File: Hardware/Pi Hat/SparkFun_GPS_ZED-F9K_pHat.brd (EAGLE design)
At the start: 65 x 56.5 mm, 70 parts, among them J1 QWIIC_RIGHT_ANGLE, J2 RASPBERRYPI-40-PIN-GPIO_PTH_N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, J4 U.FL, U1 UBLOX_ZED_F9K, U3 TRIPLE_BUFFER_74LVC3G07

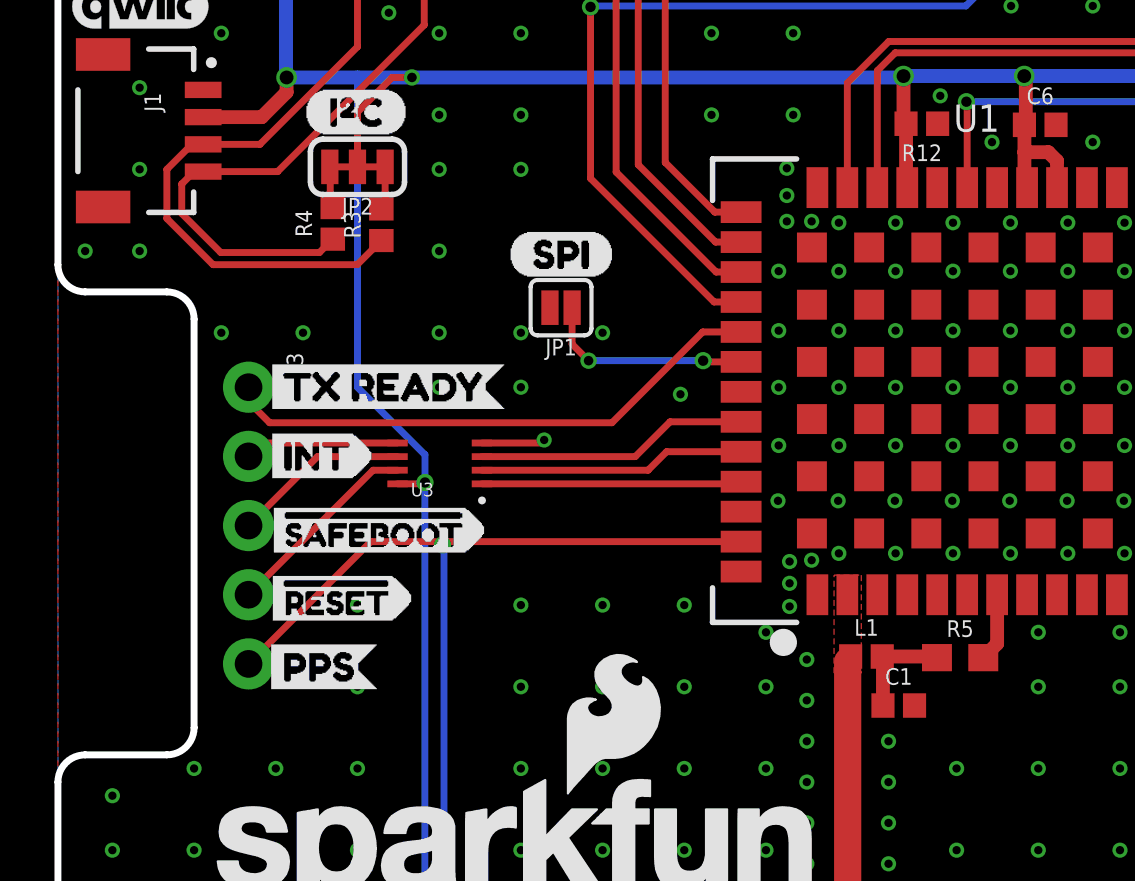
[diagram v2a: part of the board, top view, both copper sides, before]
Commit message: Replaces some 0402 components for 0603 on the pi-hat
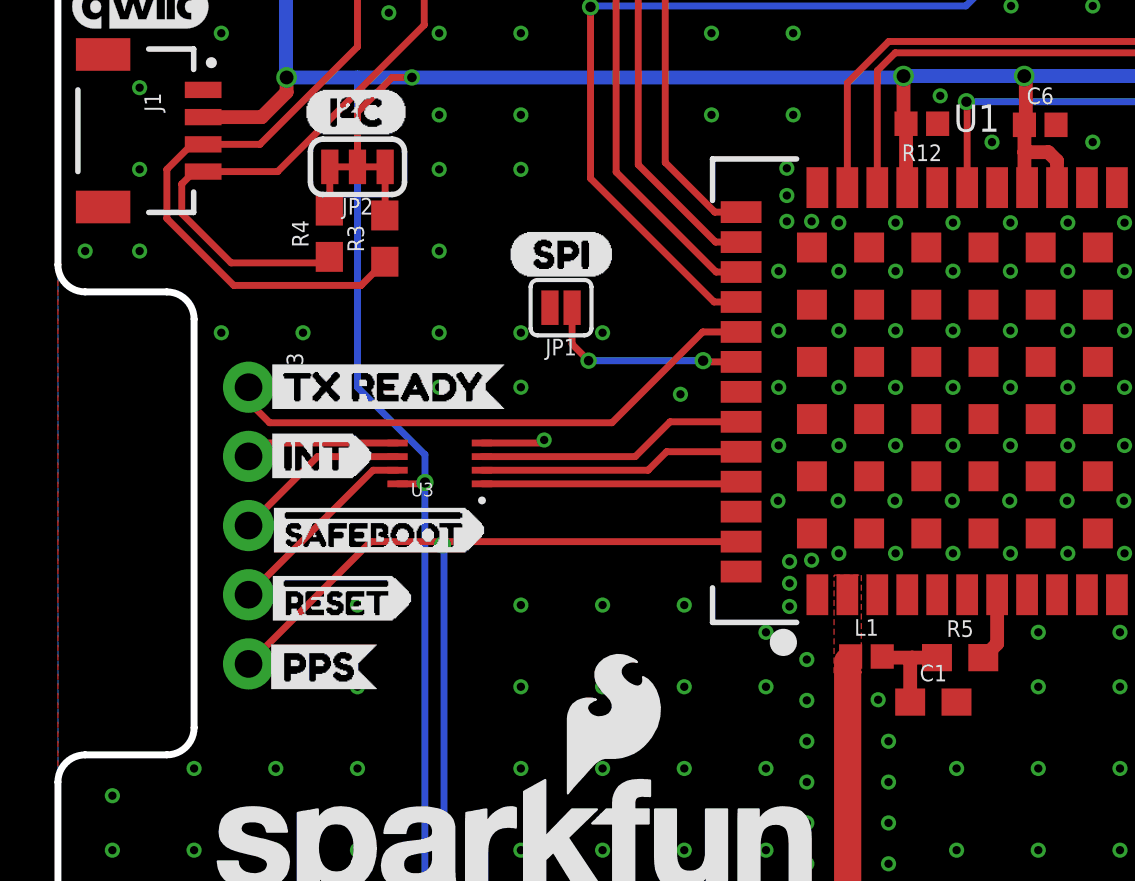
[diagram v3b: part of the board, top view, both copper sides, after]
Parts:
- C1: device SparkFun-Capacitors:0402 -> SparkFun-Capacitors:0603
- R3, R4: value 2.2K -> 2.2k; device SparkFun-Resistors:0402 -> SparkFun-Resistors:0603
- moved C1 1.28 mm to (32.1, 21.4)
- moved R3 0.52 mm to (12.0, 38.5)
- moved R4 0.40 mm to (9.97, 38.6)
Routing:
- net GND: vias 297 -> 298
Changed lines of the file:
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@@
 <setting verticaltext="up"/>
 </settings>
-<grid distance="1" unitdist="mm" unit="mm" style="lines" multiple="1" display="yes" altdistance="0.25" altunitdist="mm" altunit="mm"/>
+<grid distance="0.05" unitdist="inch" unit="inch" style="lines" multiple="1" display="yes" altdistance="0.005" altunitdist="inch" altunit="inch"/>
 <layers>
 <layer number="1" name="Top" color="4" fill="1" visible="yes" active="yes"/>
@@
 <layer number="27" name="tValues" color="7" fill="1" visible="no" active="yes"/>
 <layer number="28" name="bValues" color="7" fill="1" visible="no" active="yes"/>
-<layer number="29" name="tStop" color="7" fill="3" visible="yes" active="yes"/>
-<layer number="30" name="bStop" color="7" fill="6" visible="yes" active="yes"/>
+<layer number="29" name="tStop" color="7" fill="3" visible="no" active="yes"/>
+<layer number="30" name="bStop" color="7" fill="6" visible="no" active="yes"/>
 <layer number="31" name="tCream" color="7" fill="4" visible="no" active="yes"/>
 <layer number="32" name="bCream" color="7" fill="5" visible="no" active="yes"/>
@@
 <layer number="37" name="tTest" color="7" fill="1" visible="no" active="yes"/>
 <layer number="38" name="bTest" color="7" fill="1" visible="no" active="yes"/>
-<layer number="39" name="tKeepout" color="4" fill="11" visible="yes" active="yes"/>
-<layer number="40" name="bKeepout" color="1" fill="11" visible="yes" active="yes"/>
-<layer number="41" name="tRestrict" color="4" fill="10" visible="yes" active="yes"/>
-<layer number="42" name="bRestrict" color="1" fill="10" visible="yes" active="yes"/>
+<layer number="39" name="tKeepout" color="4" fill="11" visible="no" active="yes"/>
+<layer number="40" name="bKeepout" color="1" fill="11" visible="no" active="yes"/>
+<layer number="41" name="tRestrict" color="4" fill="10" visible="no" active="yes"/>
+<layer number="42" name="bRestrict" color="1" fill="10" visible="no" active="yes"/>
 <layer number="43" name="vRestrict" color="2" fill="10" visible="no" active="yes"/>
 <layer number="44" name="Drills" color="7" fill="1" visible="no" active="yes"/>
@@
 <layer number="115" name="ReferenceISLANDS" color="7" fill="1" visible="no" active="no"/>
 <layer number="116" name="Patch_BOT" color="9" fill="4" visible="no" active="no"/>
-<layer number="117" name="PM_Ref" color="26" fill="1" visible="no" active="yes"/>
+<layer number="117" name="PM_Ref" color="26" fill="1" visible="yes" active="yes"/>
 <layer number="118" name="Rect_Pads" color="7" fill="1" visible="no" active="no"/>
-<layer number="119" name="PF_Ref" color="31" fill="1" visible="no" active="yes"/>
-<layer number="120" name="WFL_Ref" color="25" fill="1" visible="no" active="yes"/>
+<layer number="119" name="PF_Ref" color="31" fill="1" visible="yes" active="yes"/>
+<layer number="120" name="WFL_Ref" color="25" fill="1" visible="yes" active="yes"/>
 <layer number="121" name="_tsilk" color="7" fill="1" visible="no" active="no"/>
 <layer number="122" name="_bsilk" color="7" fill="1" visible="no" active="no"/>
@@
 </autorouter>
 <elements>
-<element name="R3" library="SparkFun-Resistors" package="0402" value="2.2K" x="11.876" y="38.9656" smashed="yes" rot="R90">
-<attribute name="NAME" x="11.114" y="38.9656" size="0.6096" layer="25" font="vector" ratio="20" rot="R90" align="bottom-center"/>
-<attribute name="PROD_ID" value="RES-14341" x="11.876" y="38.9656" size="1.778" layer="27" font="vector" ratio="15" rot="R90" display="off"/>
-<attribute name="VALUE" value="2.2K" x="11.876" y="38.9656" size="1.778" layer="27" rot="R90" display="off"/>
-</element>
-<element name="R4" library="SparkFun-Resistors" package="0402" value="2.2K" x="10.0932" y="39.0164" smashed="yes" rot="R90">
-<attribute name="NAME" x="9.3312" y="39.0164" size="0.6096" layer="25" font="vector" ratio="20" rot="R90" align="bottom-center"/>
-<attribute name="PROD_ID" value="RES-14341" x="10.0932" y="39.0164" size="1.778" layer="27" font="vector" ratio="15" rot="R90" display="off"/>
-<attribute name="VALUE" value="2.2K" x="10.0932" y="39.0164" size="1.778" layer="27" rot="R90" display="off"/>
+<element name="R3" library="SparkFun-Resistors" package="0603" value="2.2k" x="12.003" y="38.4576" smashed="yes" rot="R90">
+<attribute name="NAME" x="11.241" y="38.4576" size="0.6096" layer="25" font="vector" ratio="20" rot="R90" align="bottom-center"/>
+<attribute name="PROD_ID" value="RES-08272" x="12.003" y="38.4576" size="1.778" layer="27" font="vector" ratio="15" rot="R90" display="off"/>
+<attribute name="VALUE" value="2.2k" x="12.003" y="38.4576" size="1.778" layer="27" rot="R90" display="off"/>
+</element>
+<element name="R4" library="SparkFun-Resistors" package="0603" value="2.2k" x="9.9662" y="38.6354" smashed="yes" rot="R90">
+<attribute name="NAME" x="9.2042" y="38.6354" size="0.6096" layer="25" font="vector" ratio="20" rot="R90" align="bottom-center"/>
+<attribute name="PROD_ID" value="RES-08272" x="9.9662" y="38.6354" size="1.778" layer="27" font="vector" ratio="15" rot="R90" display="off"/>
+<attribute name="VALUE" value="2.2k" x="9.9662" y="38.6354" size="1.778" layer="27" rot="R90" display="off"/>
 </element>
 <element name="JP2" library="SparkFun-Jumpers" package="SMT-JUMPER_3_2-NC_TRACE_SILK" package3d_urn="urn:adsk.eagle:package:39289/1" value="JUMPER-SMT_3_2-NC_TRACE_SILK" x="11" y="41.092" smashed="yes" rot="R180">
@@
 <attribute name="REV" value="" x="1.778" y="-16.256" size="1.778" layer="27" font="vector" ratio="15" display="off"/>
 </element>
-<element name="C1" library="SparkFun-Capacitors" package="0402" value="0.1uF" x="30.876" y="21.3116" smashed="yes">
-<attribute name="NAME" x="30.876" y="22.0736" size="0.6096" layer="25" font="vector" ratio="20" align="bottom-center"/>
-<attribute name="PROD_ID" value="CAP-12416" x="30.876" y="21.3116" size="1.778" layer="27" font="vector" ratio="15" display="off"/>
-<attribute name="VALUE" x="30.876" y="20.5496" size="0.6096" layer="27" font="vector" ratio="20" align="top-center"/>
+<element name="C1" library="SparkFun-Capacitors" package="0603" value="0.1uF" x="32.146" y="21.4386" smashed="yes">
+<attribute name="NAME" x="32.146" y="22.2006" size="0.6096" layer="25" font="vector" ratio="20" align="bottom-center"/>
+<attribute name="PROD_ID" value="CAP-00810" x="32.146" y="21.4386" size="1.778" layer="27" font="vector" ratio="15" display="off"/>
+<attribute name="VALUE" x="32.146" y="20.6766" size="0.6096" layer="27" font="vector" ratio="20" align="top-center"/>
 </element>
 <element name="L1" library="SparkFun-Coils" package="0402" value="3.9NH" x="29.6892" y="23.1114" smashed="yes">
@@
 <via x="46.75" y="4" extent="1-16" drill="0.3048"/>
 <via x="46.75" y="7" extent="1-16" drill="0.3048"/>
+<via x="30.119" y="21.524" extent="1-16" drill="0.3048"/>
 </signal>
 <signal name="3.3V">
@@
 <contactref element="R3" pad="2"/>
 <contactref element="JP2" pad="1"/>
-<wire x1="11.876" y1="39.5456" x2="12.016" y2="39.6856" width="0.254" layer="1"/>
-<wire x1="12.016" y1="39.6856" x2="12.016" y2="41.092" width="0.254" layer="1"/>
+<wire x1="12.016" y1="41.092" x2="12.016" y2="39.3206" width="0.254" layer="1"/>
+<wire x1="12.016" y1="39.3206" x2="12.003" y2="39.3076" width="0.254" layer="1"/>
 </signal>
 <signal name="N$3">
 <contactref element="JP2" pad="3"/>
 <contactref element="R4" pad="2"/>
-<wire x1="10.0932" y1="39.5964" x2="10" y2="39.6896" width="0.254" layer="1"/>
-<wire x1="10" y1="39.6896" x2="10" y2="41.076" width="0.254" layer="1"/>
 <wire x1="10" y1="41.076" x2="9.984" y2="41.092" width="0.254" layer="1"/>
+<wire x1="9.984" y1="41.092" x2="9.984" y2="39.5032" width="0.254" layer="1"/>
+<wire x1="9.984" y1="39.5032" x2="9.9662" y2="39.4854" width="0.254" layer="1"/>
 </signal>
 <signal name="RF_IN">
@@
 <contactref element="R5" pad="1"/>
 <wire x1="32.2796" y1="23.0702" x2="32.2384" y2="23.1114" width="0.508" layer="1"/>
-<wire x1="32.2384" y1="23.1114" x2="30.2692" y2="23.1114" width="0.508" layer="1"/>
-<wire x1="30.296" y1="21.3116" x2="30.296" y2="23.0846" width="0.508" layer="1"/>
-<wire x1="30.296" y1="23.0846" x2="30.2692" y2="23.1114" width="0.508" layer="1"/>
+<wire x1="32.2796" y1="23.0702" x2="31.369" y2="23.0702" width="0.508" layer="1"/>
+<wire x1="31.369" y1="23.0702" x2="30.3104" y2="23.0702" width="0.508" layer="1"/>
+<wire x1="30.3104" y1="23.0702" x2="30.2692" y2="23.1114" width="0.508" layer="1"/>
+<wire x1="31.296" y1="21.4386" x2="31.296" y2="22.9972" width="0.508" layer="1"/>
+<wire x1="31.296" y1="22.9972" x2="31.369" y2="23.0702" width="0.508" layer="1"/>
 </signal>
 <signal name="V_RF">
@@
 <wire x1="5.0024" y1="40.918" x2="4.5466" y2="40.4622" width="0.254" layer="1"/>
 <wire x1="4.5466" y1="40.4622" x2="4.5466" y2="39.378" width="0.254" layer="1"/>
-<wire x1="4.5466" y1="39.378" x2="5.9784" y2="37.9462" width="0.254" layer="1"/>
-<wire x1="5.9784" y1="37.9462" x2="9.603" y2="37.9462" width="0.254" layer="1"/>
-<wire x1="9.603" y1="37.9462" x2="10.0932" y2="38.4364" width="0.254" layer="1"/>
+<wire x1="4.5466" y1="39.378" x2="6.3594" y2="37.5652" width="0.254" layer="1"/>
+<wire x1="9.9662" y1="37.7854" x2="9.746" y2="37.5652" width="0.254" layer="1"/>
+<wire x1="9.746" y1="37.5652" x2="6.3594" y2="37.5652" width="0.254" layer="1"/>
 </signal>
 <signal name="QWIIC_SDA">
@@
 <wire x1="5.334" y1="41.918" x2="4.918" y2="41.918" width="0.254" layer="1"/>
 <wire x1="4.918" y1="41.918" x2="4" y2="41" width="0.254" layer="1"/>
-<wire x1="11.876" y1="38.3856" x2="10.9904" y2="37.5" width="0.254" layer="1"/>
-<wire x1="10.9904" y1="37.5" x2="5.6952" y2="37.5" width="0.254" layer="1"/>
 <wire x1="4" y1="41" x2="4" y2="39.1952" width="0.254" layer="1"/>
-<wire x1="4" y1="39.1952" x2="5.6952" y2="37.5" width="0.254" layer="1"/>
+<wire x1="4" y1="39.1952" x2="6.4572" y2="36.738" width="0.254" layer="1"/>
+<wire x1="11.1334" y1="36.738" x2="12.003" y2="37.6076" width="0.254" layer="1"/>
+<wire x1="6.4572" y1="36.738" x2="11.1334" y2="36.738" width="0.254" layer="1"/>
 </signal>
 <signal name="5V">

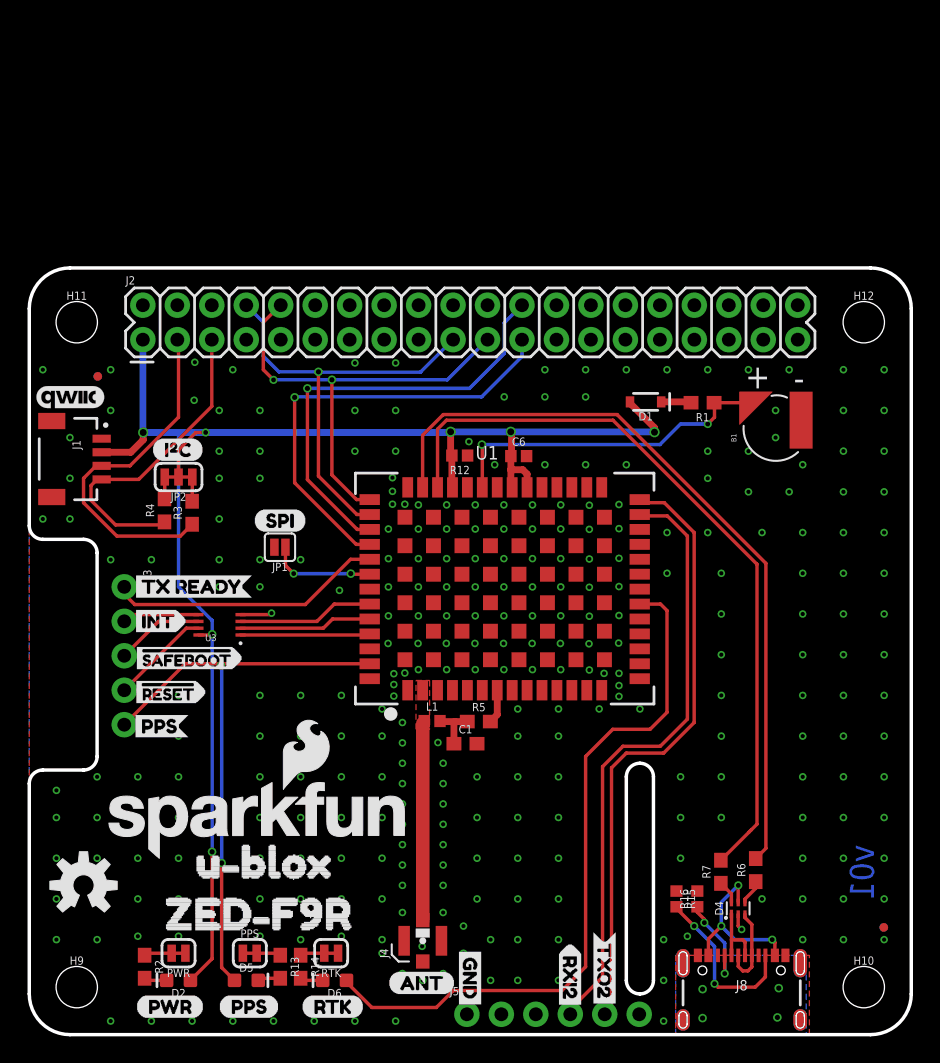
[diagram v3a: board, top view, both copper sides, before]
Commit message: Adds F9R datasheets, updates design with wheel ticks, direction pins, and adds 33 Ohm filtering resistors to all I/O
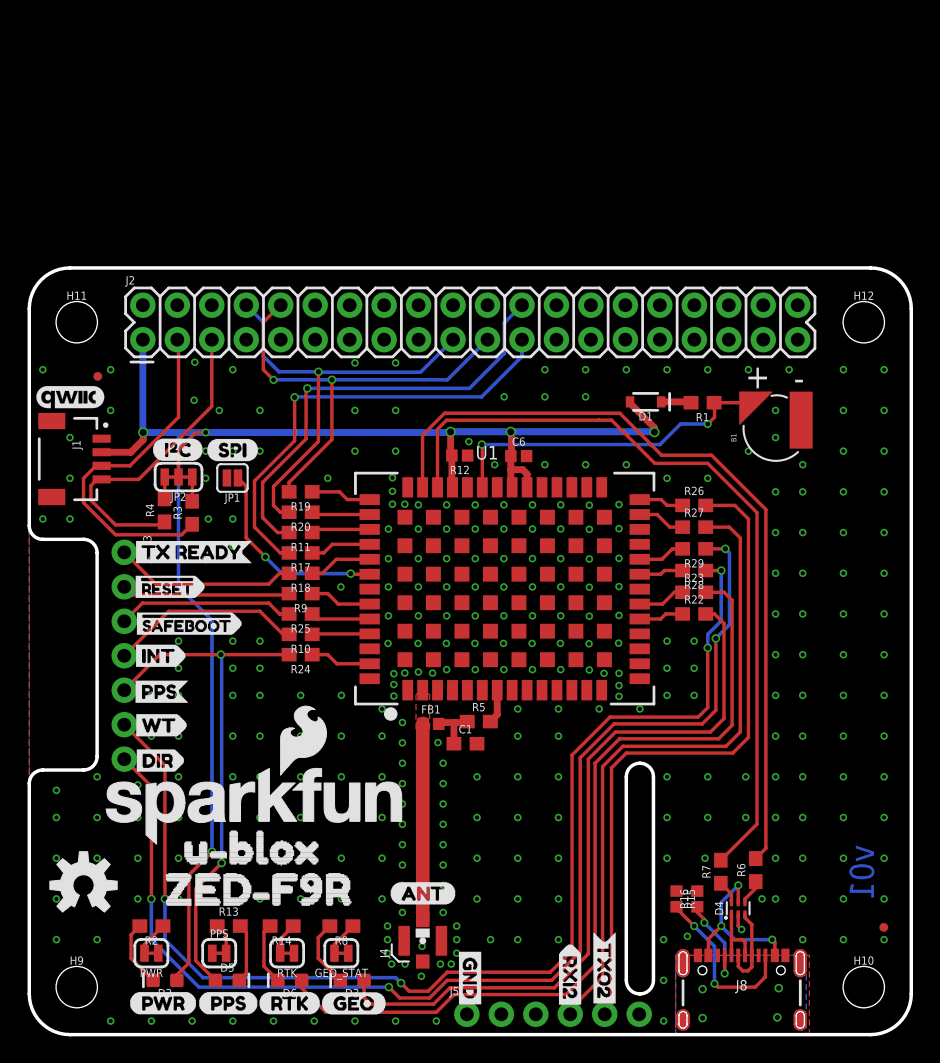
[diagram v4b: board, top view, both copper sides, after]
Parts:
- removed L1: 3.9NH, SparkFun-Coils:0402
- removed U3: TRIPLE_BUFFER_74LVC3G07, classified:SOP_8-PIN
- added D3: BLUE, SparkFun-LED:LED-0603
- added FB1: FERRITE_BEAD-120_OHM-0402, SparkFun-Coils:0402
- added GEO_STAT: JUMPER-SMT_2_NC_TRACE_SILK, SparkFun-Jumpers:SMT-JUMPER_2_NC_TRACE_SILK
- added R10, R11, R17, R18, R19, R20, R22, R23, R24, R25, R26, R27, R28, R29, R9: 33, SparkFun-Resistors:0603
- added R8: 1k, SparkFun-Resistors:0603
- added U$22: (no value), wt_dir:DIR1
- added U$23: (no value), wt_dir:WT0
- added U$27: (no value), wt_dir:DIR3
- added U$28: (no value), wt_dir:WT2
- added U$29: (no value), geo:GEO0
- C1: value 0.1uF -> 47pF
- J3: device SparkFun-Connectors:1X05_NO_SILK -> SparkFun-Connectors:1X07_NO_SILK
- R5: value 20 -> 10
- U1: value UBLOX_ZED_F9K -> UBLOX_ZED_F9R; device classified:UBLOX_ZED_F9K -> classified:UBLOX_ZED_F9R
- moved U$7 7.75 mm to (7.20, 33.0)
- moved U$8 7.74 mm to (13.2, 33.0)
- moved U$21 6.60 mm to (26.5, 10.4)
- moved U$24 6.27 mm to (13.0, 43.1)
- moved JP1 6.19 mm to (15.0, 41.0)
- moved R13 4.84 mm to (14.7, 8.00), turned to 0 degrees
- moved R14 3.31 mm to (18.6, 8.00), turned to 180 degrees
- moved D6 3.30 mm to (19.2, 4.00)
- moved RTK 3.25 mm to (19.0, 6.00)
- moved U$5 3.19 mm to (16.9, 2.31)
- moved R2 3.04 mm to (9.00, 8.00), turned to 180 degrees
- moved U$11 2.56 mm to (11.7, 27.9)
- moved U$1 2.56 mm to (7.35, 27.9)
- moved J3 2.54 mm to (7.00, 35.5)
- moved U$12 2.54 mm to (11.8, 25.3)
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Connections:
- removed net !RESET_IN: U1.P49, U3.P3
- removed net !RESET_OUT: J3.4, U3.P7
- removed net !SAFEBOOT_IN: J3.3, U3.P6
- removed net !SAFEBOOT_OUT: U1.P50, U3.P2
- removed net INT_IN: U1.P51, U3.P1
- removed net INT_OUT: J3.2, U3.P5
- new net !RESET: J3.2, R9.2
- new net !SAFEBOOT: J3.3, R25.2
- new net DIR: J3.7, R29.1
- new net GEOF_STAT: D3.A, R22.2
- new net INT: J3.4, R10.2
- new net N$13: R9.1, U1.P49
- new net N$16: GEO_STAT.2, R8.1
- new net N$17: D3.C, R8.2
- new net N$19: R17.1, U1.P45
- new net N$20: R18.1, U1.P46
- new net N$21: R19.1, U1.P42
- new net N$26: R20.1, U1.P43
- new net N$28: R22.1, U1.P19
- new net N$29: R23.1, U1.P20
- new net N$30: R24.1, U1.P53
- new net N$31: R25.1, U1.P50
- new net N$32: R26.1, U1.P27
- new net N$33: R27.1, U1.P26
- new net N$34: R28.2, U1.P22
- new net N$35: R29.2, U1.P23
- new net WT: J3.6, R28.1
- net 3.3V: no longer U3.P8
- net GND: now also GEO_STAT.1; no longer U3.P4
- net N$14: now also R10.1, U1.P51; no longer U1.P22
- net N$15: now also R11.1, U1.P44; no longer U1.P23
- net N$5: now also FB1.2; no longer L1.2
- net PPS: now also R24.2; no longer U1.P53
- net RF_IN: now also FB1.1; no longer L1.1
- net RTK_STAT: now also R23.2; no longer U1.P20
- net RXI/MOSI: now also R20.2; no longer U1.P43
- net RXI2: now also R27.2; no longer U1.P26
- net SCL/CLK: now also R17.2; no longer U1.P45
- net SDA/!CS: now also R11.2; no longer U1.P44
- net TXO/MISO: now also R19.2; no longer U1.P42
- net TXO2: now also R26.2; no longer U1.P27
- net TX_READY: now also R18.2; no longer U1.P46
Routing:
- net DIR: track 0.00 -> 88.6 mm, vias 0 -> 4
- net WT: track 0.00 -> 87.4 mm, vias 0 -> 4
- net GEOF_STAT: track 0.00 -> 53.8 mm
- net INT: track 0.00 -> 14.3 mm
- net !SAFEBOOT: track 0.00 -> 13.0 mm
- net !RESET: track 0.00 -> 12.4 mm
- net !RESET_IN: track 10.0 -> 0.00 mm
- net !SAFEBOOT_OUT: track 9.80 -> 0.00 mm
- net RTK_STAT: track 52.3 -> 61.9 mm
- net INT_IN: track 9.55 -> 0.00 mm
- net !RESET_OUT: track 7.36 -> 0.00 mm
- net D_SEL: track 7.82 -> 14.9 mm
- net TX_READY: track 20.3 -> 13.5 mm
- net !SAFEBOOT_IN: track 6.52 -> 0.00 mm
- net INT_OUT: track 5.67 -> 0.00 mm
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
